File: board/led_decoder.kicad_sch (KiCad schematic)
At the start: 1 part, among them U1 74VHC138FT

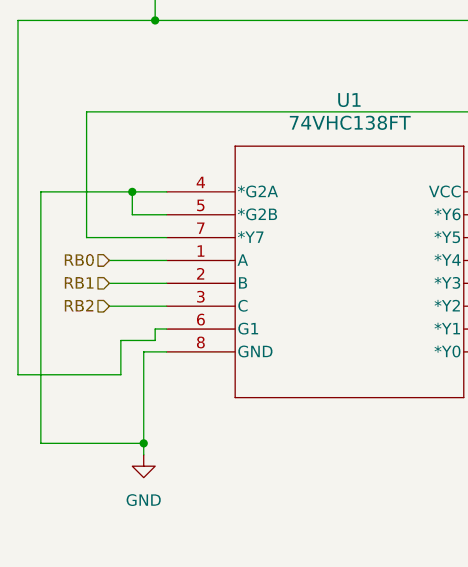
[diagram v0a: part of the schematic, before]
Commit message: Added Rotary Encoder
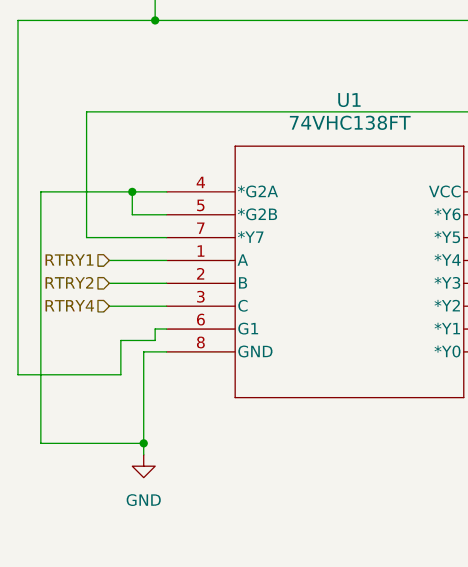
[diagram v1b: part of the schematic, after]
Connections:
- net RB0 renamed RTRY1
- net RB1 renamed RTRY2
- net RB2 renamed RTRY4
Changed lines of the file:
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@@
 		)
 	)
-	(hierarchical_label "RB2"
+	(hierarchical_label "RTRY4"
 		(shape input)
 		(at 86.36 87.63 180)
@@
 		)
 	)
-	(hierarchical_label "RB1"
+	(hierarchical_label "RTRY2"
 		(shape input)
 		(at 86.36 85.09 180)
@@
 		)
 	)
-	(hierarchical_label "RB0"
+	(hierarchical_label "RTRY1"
 		(shape input)
 		(at 86.36 82.55 180)

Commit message: Selection LEDs
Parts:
- added D12, D13, D4, D5, D6, D8: Orange, LED_SMD:LED_0603_1608Metric_Pad1.05x0.95mm_HandSolder, symbol Device:LED
- added D14, D15, D16, D17, D18: Blue, LED_SMD:LED_0603_1608Metric_Pad1.05x0.95mm_HandSolder, symbol Device:LED
- added Q1, Q10, Q11, Q2, Q3, Q4, Q5, Q6, Q7, Q8, Q9: PMOS, symbol Simulation_SPICE:PMOS
- added R12, R13, R20, R21, R22: 1120, symbol Device:R_US
- added R4, R5, R6, R7, R8, R9: 1k, symbol Device:R_US
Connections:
- net +3.3V: now also Q10.3 (S), Q11.3 (S), Q7.3 (S), Q8.3 (S), Q9.3 (S)
- net BL_EN: now also Q5.3 (S)
- net BR_EN: now also Q1.3 (S)
- net FL_EN: now also Q6.3 (S)
- net FR_EN: now also Q3.3 (S)
- net GND: now also R12.1, R13.1, R20.1, R21.1, R22.1, R4.1, R5.1, R6.1, R7.1, R8.1, R9.1
- net ML_EN: now also Q2.3 (S)
- net MR_EN: now also Q4.3 (S)
- net Spare2: now reaches U1.10 (*Y5)
- net Spare2: now also Q10.2 (G)
- net Spare1: now reaches U1.11 (*Y4)
- net Spare1: now also Q9.2 (G)
- net BackCam: now reaches U1.12 (*Y3)
- net BackCam: now also Q8.2 (G)
- net LeftMast: now reaches U1.13 (*Y2)
- net LeftMast: now also Q7.2 (G)
- net Rightmast: now reaches U1.14 (*Y1)
- net Off: now reaches U1.15 (*Y0)
- net Wheels: now reaches U1.9 (*Y6)
- net Wheels: now also Q1.2 (G), Q2.2 (G), Q3.2 (G), Q4.2 (G), Q5.2 (G), Q6.2 (G)
- new net: D18.1 (K), R22.2
- new net: D6.2 (A), Q2.1 (D)
- new net: D15.1 (K), R13.2
- new net: D15.2 (A), Q8.1 (D)
- new net: D17.1 (K), R21.2
- new net: D5.1 (K), R4.2
- new net: D16.1 (K), R20.2
- new net: D4.1 (K), R5.2
- new net: D4.2 (A), Q5.1 (D)
- new net: D5.2 (A), Q1.1 (D)
- new net: D6.1 (K), R6.2
- new net: D8.2 (A), Q3.1 (D)
- new net: D14.1 (K), R12.2
- new net: D18.2 (A), Q11.1 (D)
- new net: D8.1 (K), R9.2
- new net: D13.1 (K), R7.2
- new net: D17.2 (A), Q10.1 (D)
- new net: D12.1 (K), R8.2
- new net: D12.2 (A), Q4.1 (D)
- new net: D16.2 (A), Q9.1 (D)
- new net: D14.2 (A), Q7.1 (D)
- new net: D13.2 (A), Q6.1 (D)
- new net RightMast: Q11.2 (G)

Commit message: Fan, Light, Buck
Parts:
- Q1, Q10, Q11, Q2, Q3, Q4, Q5, Q6, Q7, Q8, Q9: value PMOS -> AO3401A
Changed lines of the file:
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@@
 			)
 		)
-		(property "Value" "PMOS"
+		(property "Value" "AO3401A"
 			(at 265.43 97.7899 0)
 			(effects
@@
 			)
 		)
-		(property "Value" "PMOS"
+		(property "Value" "AO3401A"
 			(at 189.23 38.0999 0)
 			(effects
@@
 		(fields_autoplaced yes)
 		(property "Reference" "Q8"
-			(at 84.8934 138.076 0)
+			(at 83.82 138.076 0)
 			(effects
 				(font
@@
 			)
 		)
-		(property "Value" "PMOS"
-			(at 84.8934 140.616 0)
+		(property "Value" "AO3401A"
+			(at 83.82 140.616 0)
 			(effects
 				(font
@@
 		(fields_autoplaced yes)
 		(property "Reference" "Q10"
-			(at 156.2084 137.7533 0)
+			(at 156.21 137.7533 0)
 			(effects
 				(font
@@
 			)
 		)
-		(property "Value" "PMOS"
-			(at 156.2084 140.2933 0)
+		(property "Value" "AO3401A"
+			(at 156.21 140.2933 0)
 			(effects
 				(font
@@
 		(fields_autoplaced yes)
 		(property "Reference" "Q9"
-			(at 120.3896 137.4306 0)
+			(at 119.38 137.4306 0)
 			(effects
 				(font
@@
 			)
 		)
-		(property "Value" "PMOS"
-			(at 120.3896 139.9706 0)
+		(property "Value" "AO3401A"
+			(at 119.38 139.9706 0)
 			(effects
 				(font
@@
 			)
 		)
-		(property "Value" "PMOS"
+		(property "Value" "AO3401A"
 			(at 50.8 139.6999 0)
 			(effects
@@
 			)
 		)
-		(property "Value" "PMOS"
+		(property "Value" "AO3401A"
 			(at 189.23 97.7899 0)
 			(effects
@@
 			)
 		)
-		(property "Value" "PMOS"
+		(property "Value" "AO3401A"
 			(at 231.14 99.0599 0)
 			(effects
@@
 			)
 		)
-		(property "Value" "PMOS"
+		(property "Value" "AO3401A"
 			(at 260.35 38.0999 0)
 			(effects
@@
 			)
 		)
-		(property "Value" "PMOS"
+		(property "Value" "AO3401A"
 			(at 227.33 38.0999 0)
 			(effects
@@
 			)
 		)
-		(property "Value" "PMOS"
+		(property "Value" "AO3401A"
 			(at 50.8 81.2799 0)
 			(effects

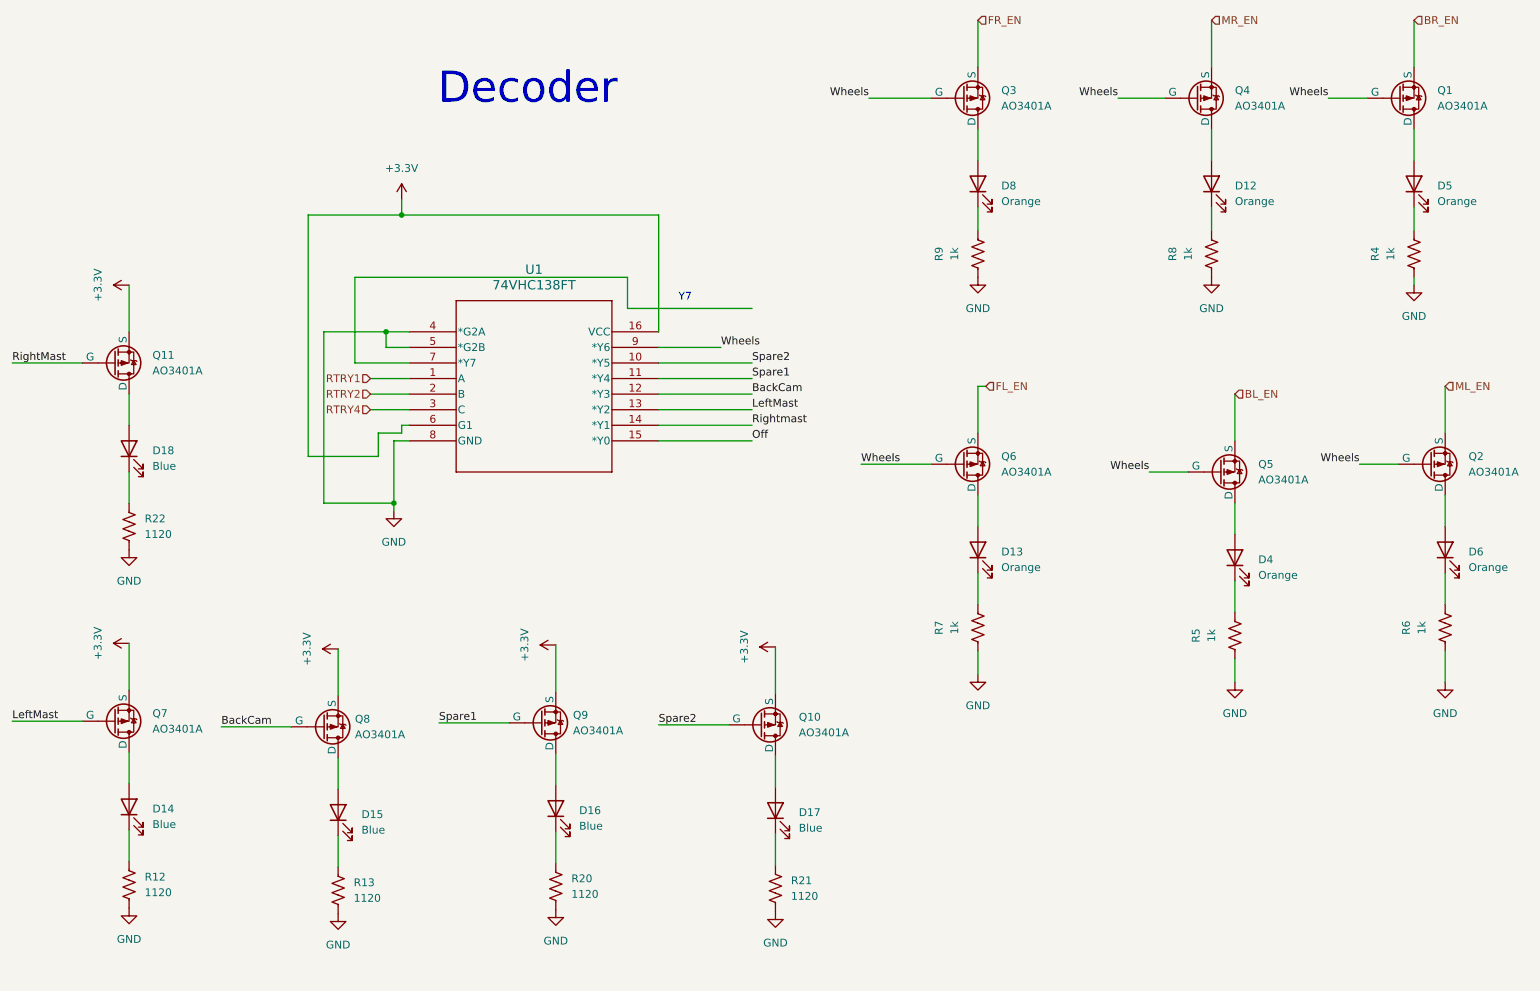
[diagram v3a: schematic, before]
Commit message: Added most Footprints, Schematic review touch up
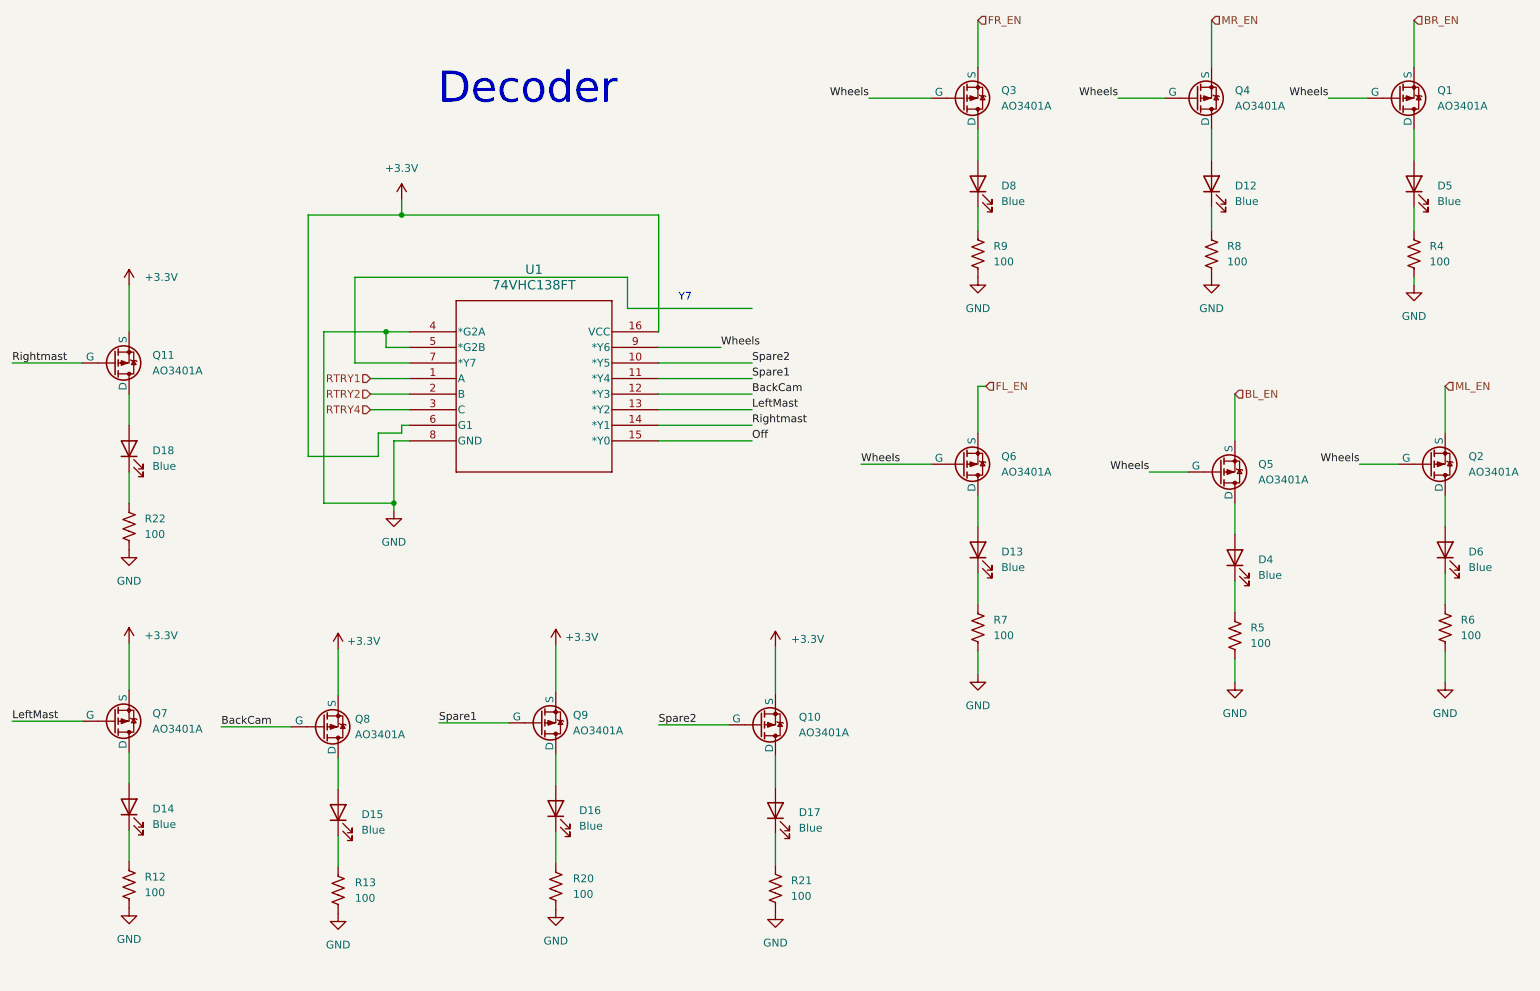
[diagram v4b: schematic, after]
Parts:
- D12, D13, D4, D5, D6, D8: value Orange -> Blue
- Q1, Q10, Q11, Q2, Q3, Q4, Q5, Q6, Q7, Q8, Q9: footprint (none) -> CoreBoard:SOT-23-3L_AOS-L
- R12, R13, R20, R21, R22: value 1120 -> 100; footprint (none) -> Resistor_SMD:R_0603_1608Metric_Pad0.98x0.95mm_HandSolder
- R4, R5, R6, R7, R8, R9: value 1k -> 100; footprint (none) -> Resistor_SMD:R_0603_1608Metric_Pad0.98x0.95mm_HandSolder
- U1: footprint TSSOP16B_TOS -> CoreBoard:TSSOP16B_TOS-L
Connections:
- net RightMast is gone; now on net Rightmast: Q11.2 (G)

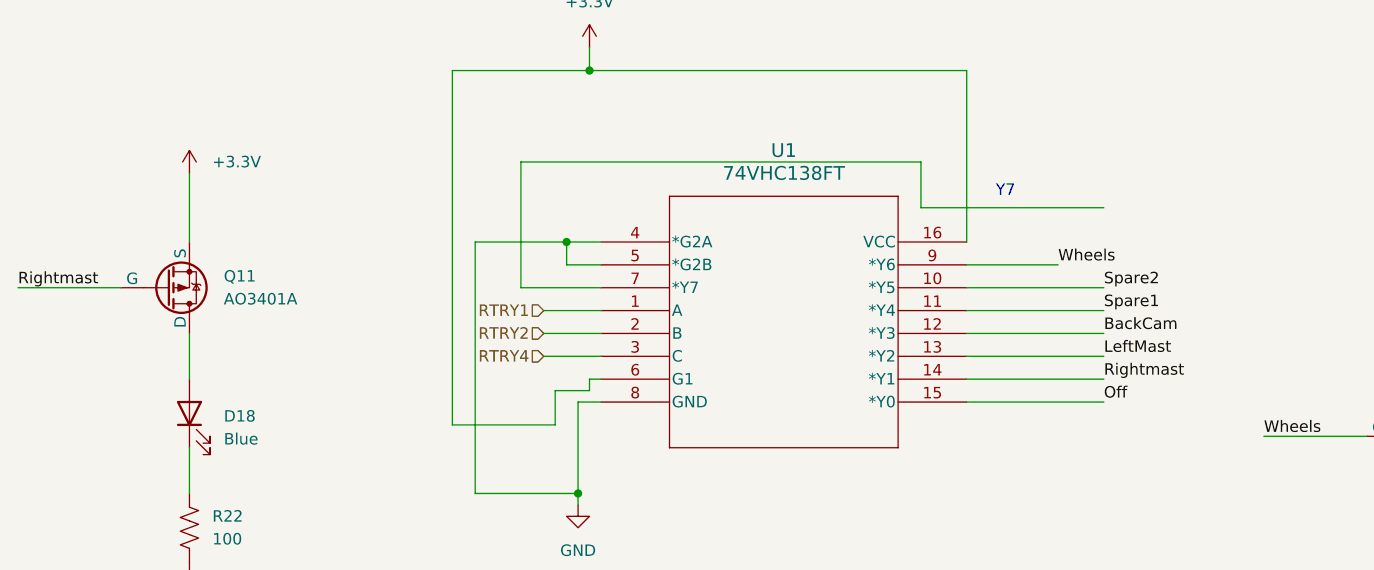
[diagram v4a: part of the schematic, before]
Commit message: routed core board
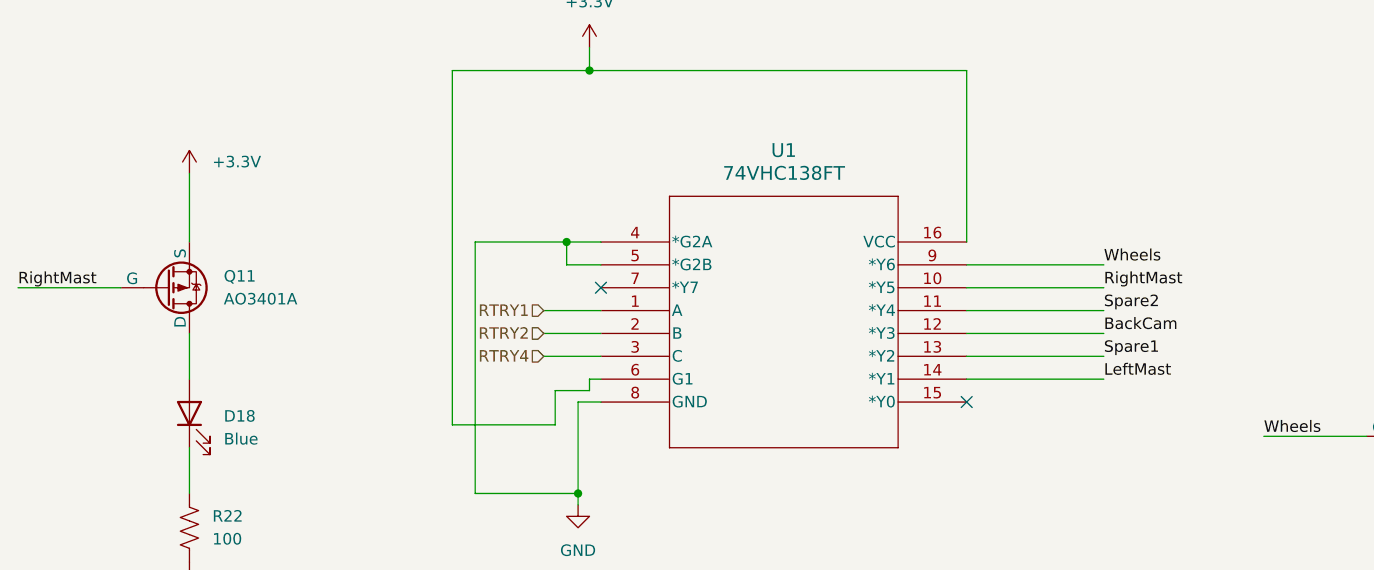
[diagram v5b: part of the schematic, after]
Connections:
- net LeftMast: now also U1.14 (*Y1); no longer U1.13 (*Y2)
- net Spare1: now also U1.13 (*Y2); no longer U1.11 (*Y4)
- net Spare2: now also U1.11 (*Y4); no longer U1.10 (*Y5)
- net Off: no longer names the net of U1.15 (*Y0)
- net Rightmast renamed RightMast
- net RightMast: now also U1.10 (*Y5); no longer U1.14 (*Y1)
- no-connect marks 0 -> 2
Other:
- note removed: "Y7"
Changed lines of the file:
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@@
 	(generator_version "9.0")
 	(paper "A4")
-	(text "Y7\n"
-		(exclude_from_sim no)
-		(at 137.668 69.342 0)
-		(effects
-			(font
-				(size 1.27 1.27)
-			)
-		)
-	)
 	(text "Decoder"
 		(exclude_from_sim no)
@@
 		(color 0 0 0 0)
 	)
+	(no_connect
+		(at 92.71 80.01)
+	)
+	(no_connect
+		(at 133.35 92.71)
+	)
 	(wire
 		(pts
@@
 	(wire
 		(pts
-			(xy 83.82 66.04) (xy 83.82 80.01)
-		)
-		(stroke
-			(width 0)
-			(type default)
-		)
-	)
-	(wire
-		(pts
-			(xy 83.82 66.04) (xy 128.27 66.04)
-		)
-		(stroke
-			(width 0)
-			(type default)
-		)
-	)
-	(wire
-		(pts
 			(xy 133.35 85.09) (xy 148.59 85.09)
 		)
@@
 	(wire
 		(pts
-			(xy 133.35 77.47) (xy 143.51 77.47)
+			(xy 133.35 77.47) (xy 148.59 77.47)
 		)
 		(stroke
@@
 	(wire
 		(pts
-			(xy 92.71 80.01) (xy 83.82 80.01)
-		)
-		(stroke
-			(width 0)
-			(type default)
-		)
-	)
-	(wire
-		(pts
 			(xy 81.0834 157.1261) (xy 81.0834 162.2061)
 		)
@@
 	(wire
 		(pts
-			(xy 128.27 66.04) (xy 128.27 71.12)
-		)
-		(stroke
-			(width 0)
-			(type default)
-		)
-	)
-	(wire
-		(pts
 			(xy 152.3984 126.3234) (xy 152.3984 133.9434)
 		)
@@
 	(wire
 		(pts
-			(xy 133.35 92.71) (xy 148.59 92.71)
-		)
-		(stroke
-			(width 0)
-			(type default)
-		)
-	)
-	(wire
-		(pts
 			(xy 92.71 90.17) (xy 91.44 90.17)
 		)
@@
 	(wire
 		(pts
-			(xy 128.27 71.12) (xy 148.59 71.12)
-		)
-		(stroke
-			(width 0)
-			(type default)
-		)
-	)
-	(wire
-		(pts
 			(xy 46.99 97.79) (xy 46.99 102.87)
 		)
@@
 		)
 	)
-	(label "Rightmast"
+	(label "RightMast"
 		(at 27.94 80.01 0)
 		(effects
@@
 	)
 	(label "Spare2"
-		(at 148.59 80.01 0)
+		(at 148.59 82.55 0)
 		(effects
 			(font
@@
 	)
 	(label "Wheels"
-		(at 143.51 77.47 0)
+		(at 148.59 77.47 0)
 		(effects
 			(font
@@
 	)
 	(label "LeftMast"
-		(at 148.59 87.63 0)
+		(at 148.59 90.17 0)
 		(effects
 			(font
@@
 		)
 	)
-	(label "Rightmast"
-		(at 148.59 90.17 0)
+	(label "RightMast"
+		(at 148.59 80.01 0)
 		(effects
 			(font
@@
 	)
 	(label "Spare1"
-		(at 148.59 82.55 0)
+		(at 148.59 87.63 0)
 		(effects
 			(font
@@
 		(effects
 			(font
-				(size 1.27 1.27)
-			)
-			(justify left bottom)
-		)
-	)
-	(label "Off"
-		(at 148.59 92.71 0)
-		(effects
-			(font

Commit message: Preliminary changes for rev2
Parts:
- removed Q1, Q10, Q11, Q2, Q3, Q4, Q5, Q6, Q7, Q8, Q9: AO3401A, CoreBoard:SOT-23-3L_AOS-L, symbol Simulation_SPICE:PMOS
- added Q1, Q10, Q12, Q2, Q3, Q4, Q5, Q6, Q7, Q8, Q9: AO3401A, Package_TO_SOT_SMD:SOT-23, symbol Transistor_FET:AO3401A
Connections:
- net +3.3V: now also Q10.3 (D), Q12.3 (D), Q7.3 (D), Q8.3 (D), Q9.3 (D)
- net BL_EN: now also Q5.3 (D)
- net BR_EN: now also Q3.3 (D)
- net BackCam: now also Q12.1 (G)
- net FL_EN: now also Q6.3 (D)
- net FR_EN: now also Q1.3 (D)
- net LeftMast: now also Q9.1 (G)
- net ML_EN: now also Q4.3 (D)
- net MR_EN: now also Q2.3 (D)
- net RightMast: now also Q10.1 (G)
- net Spare1: now also Q8.1 (G)
- net Spare2: now also Q7.1 (G)
- net Wheels: now also Q1.1 (G), Q2.1 (G), Q3.1 (G), Q4.1 (G), Q5.1 (G), Q6.1 (G)
- net at D6.2 (A): now also Q4.2 (S)
- net at D15.2 (A): now also Q12.2 (S)
- net at D4.2 (A): now also Q5.2 (S)
- net at D5.2 (A): now also Q3.2 (S)
- net at D8.2 (A): now also Q1.2 (S)
- net at D18.2 (A): now also Q10.2 (S)
- net at D17.2 (A): now also Q7.2 (S)
- net at D12.2 (A): now also Q2.2 (S)
- net at D16.2 (A): now also Q8.2 (S)
- net at D14.2 (A): now also Q9.2 (S)
- net at D13.2 (A): now also Q6.2 (S)
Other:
- moved on the sheet: D15, D16, D17, R13, R20, R21
